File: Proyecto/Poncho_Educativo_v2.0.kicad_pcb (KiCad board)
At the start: 2 copper layers, 20 parts, among them M1 Matrix_8x8_LED, U1 MAX7219, U2 MAX7219

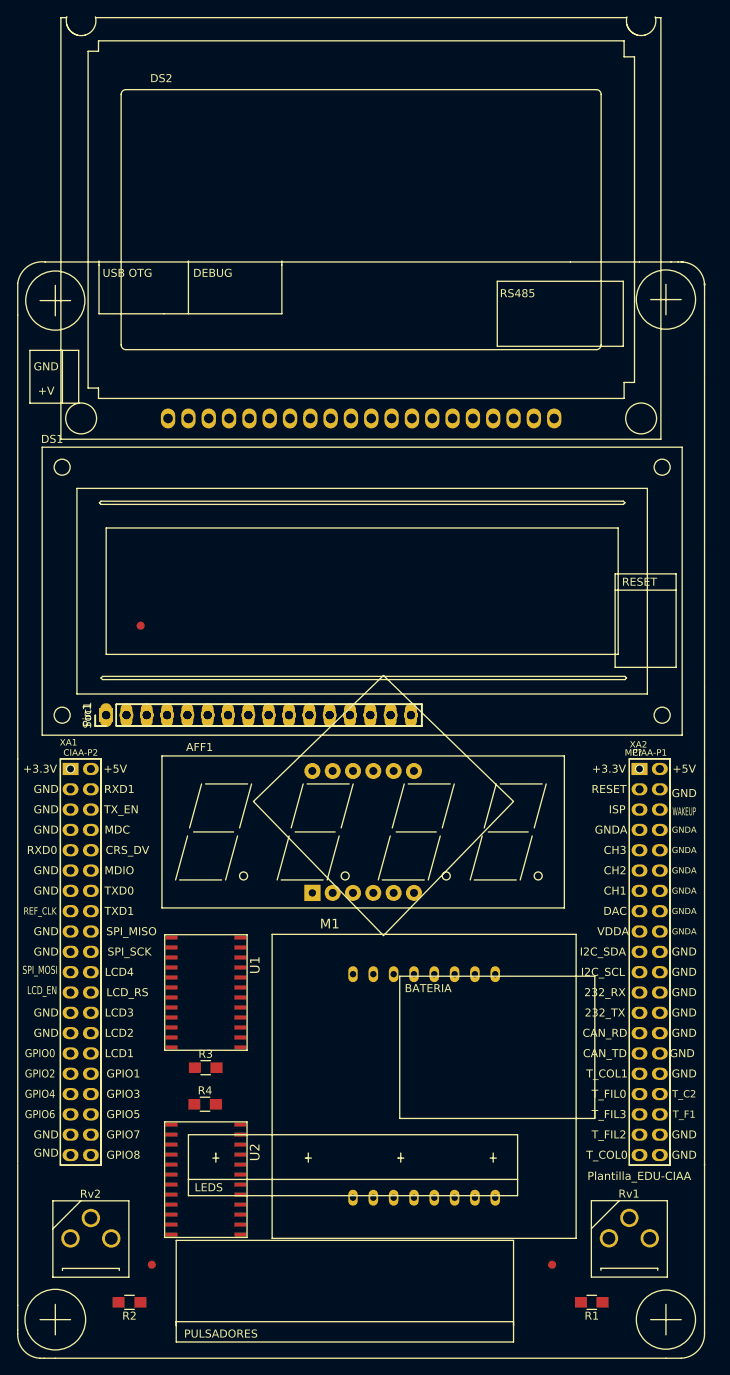
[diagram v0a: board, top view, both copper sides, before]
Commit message: Ruteo y 3D
Se realizó el ruteo completo y se agregaron modelos 3D
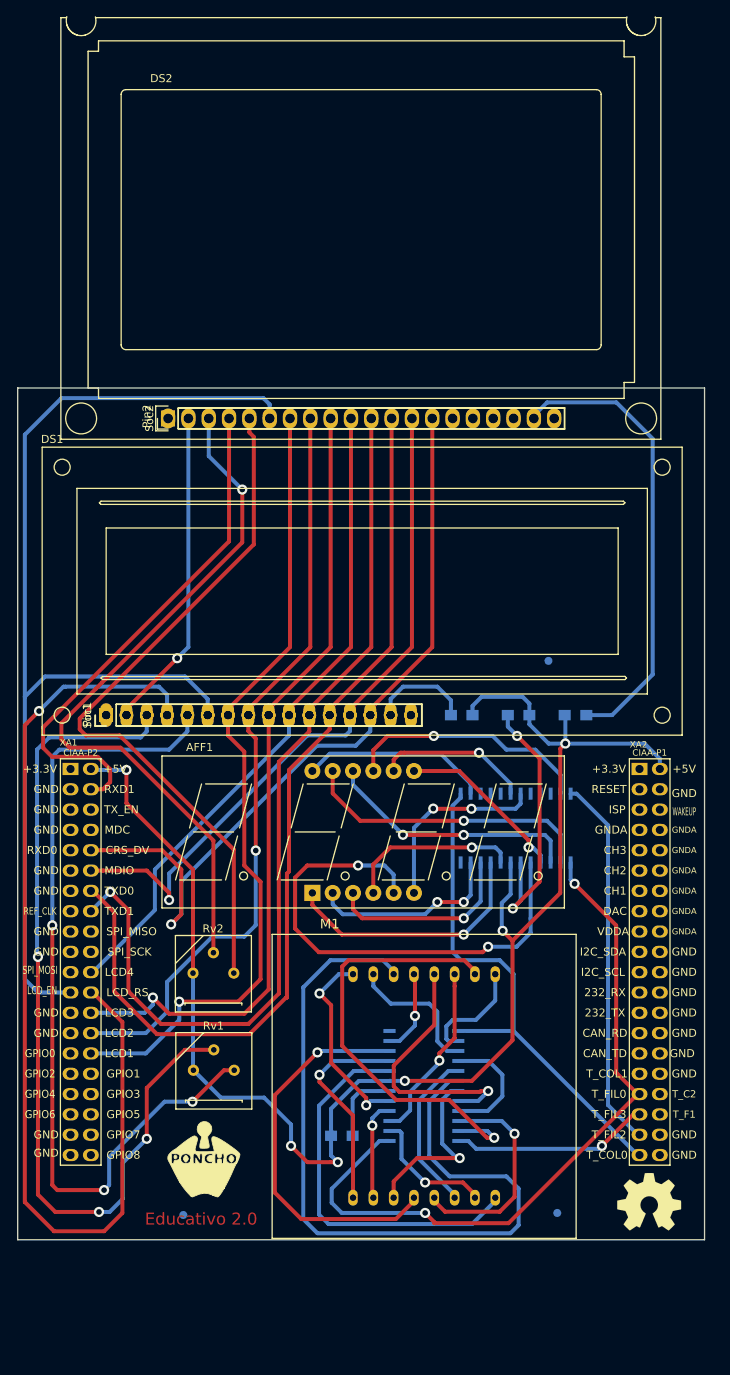
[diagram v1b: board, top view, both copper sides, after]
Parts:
- removed MP?: Plantilla_EDU-CIAA, FootPrints:Plantilla_EDU-CIAA
- added G***: LOGO, FootPrints:Logo_Poncho, F.Cu at (71.4, 163.3)
- added G***: Logo_EDU-CIAA, FootPrints:Logo_EDU-CIAA, B.Cu at (92.2, 87.0)
- added G101: Logo_OSHWA, FootPrints:Logo_OSHWA, F.Cu at (127.1, 168.5)
- added Pin2: CONN_01X20, FootPrints:Pin_Header_Straight_1x20, F.Cu at (66.9, 70.6)
- added Soc2: Socket_Strip_Straight_1x20_Pitch2.54mm, FootPrints:Socket_Strip_Straight_1x20_Pitch2.54mm, F.Cu at (66.9, 70.6)
- F1, F2, F3, R1, R2, R3, R4, U1, U2: moved to B.Cu
- moved R2 92.2 mm to (117.9, 107.7)
- moved R1 75.2 mm to (103.6, 107.7)
- moved R3 58.9 mm to (110.7, 107.7), turned to 180 degrees
- moved Rv1 56.0 mm to (72.6, 151.6)
- moved F1 51.2 mm to (114.5, 100.9)
- moved U1 43.9 mm to (110.5, 121.9), turned to 0 degrees
- moved Rv2 36.5 mm to (72.6, 139.4)
- moved U2 29.5 mm to (98.8, 154.2)
- moved R4 17.5 mm to (88.6, 160.3)
- moved F2 7.36 mm to (68.8, 170.2)
- moved F3 6.51 mm to (115.6, 169.9)
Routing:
- net +5V: track 0.00 -> 229.9 mm, vias 0 -> 7
- net /Pines Izquierdos/E: track 0.00 -> 136.1 mm
- net /Pines Izquierdos/RS1: track 0.00 -> 126.3 mm, vias 0 -> 1
- net /Pines Izquierdos/D5: track 0.00 -> 117.5 mm
- net /Pines Izquierdos/D4: track 0.00 -> 116.2 mm, vias 0 -> 1
- net Net-(DS1-Pad3): track 0.00 -> 111.5 mm, vias 0 -> 3
- net Net-(DS1-Pad5): track 0.00 -> 105.0 mm, vias 0 -> 3
- net /Pines Izquierdos/D0: track 0.00 -> 101.4 mm, vias 0 -> 1
- net /Pines Izquierdos/D2: track 0.00 -> 100.2 mm, vias 0 -> 1
- net /Pines Derechos/C2: track 0.00 -> 99.9 mm
- net /Pines Izquierdos/D1: track 0.00 -> 95.3 mm, vias 0 -> 1
- net /Pines Derechos/CLK: track 0.00 -> 90.7 mm, vias 0 -> 2
- net Net-(DS2-Pad3): track 0.00 -> 89.5 mm, vias 0 -> 1
- net Net-(DS2-Pad5): track 0.00 -> 89.0 mm
- net /Pines Izquierdos/D6: track 0.00 -> 87.7 mm, vias 0 -> 1
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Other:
- board outline added: 85.9 x 106.5 mm
- net class Default: clearance 0.2 -> 0.5; trace_width 0.25 -> 0.5; via_dia 0.6 -> 1.27; via_drill 0.4 -> 0.7
- rule trace_clearance: 0.2 -> 0.5
- rule trace_min: 0.2 -> 0.5
- rule via_min_drill: 0.3 -> 0.7
- board text added: "Diseño doble faz sin requerimientos especiales. Grilla posicionamiento: 0,508 Ancho de pista: 0,5 Diámetro de via: 0,2 Taladro de via: 1,27"
- board text added: "Educativo 2.0"
